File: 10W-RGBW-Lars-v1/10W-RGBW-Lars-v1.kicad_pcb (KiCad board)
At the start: 4 copper layers, 47.1 x 43.3 mm, 133 parts, among them J1 USB_C_Receptacle_USB2.0_16P, J101 Conn_Coaxial, J601 Screw_Terminal_01x02, SW1 SW_SPST, SW2 SW_SPST, U1 CH224D, U101 ESP32-C6FHx, U202 TPS92201, U302 TPS92201, U402 TPS92201, U502 TPS92201, U601 MB34F, U602 SY8366H, U603 XBL1117, Y1 40MHz

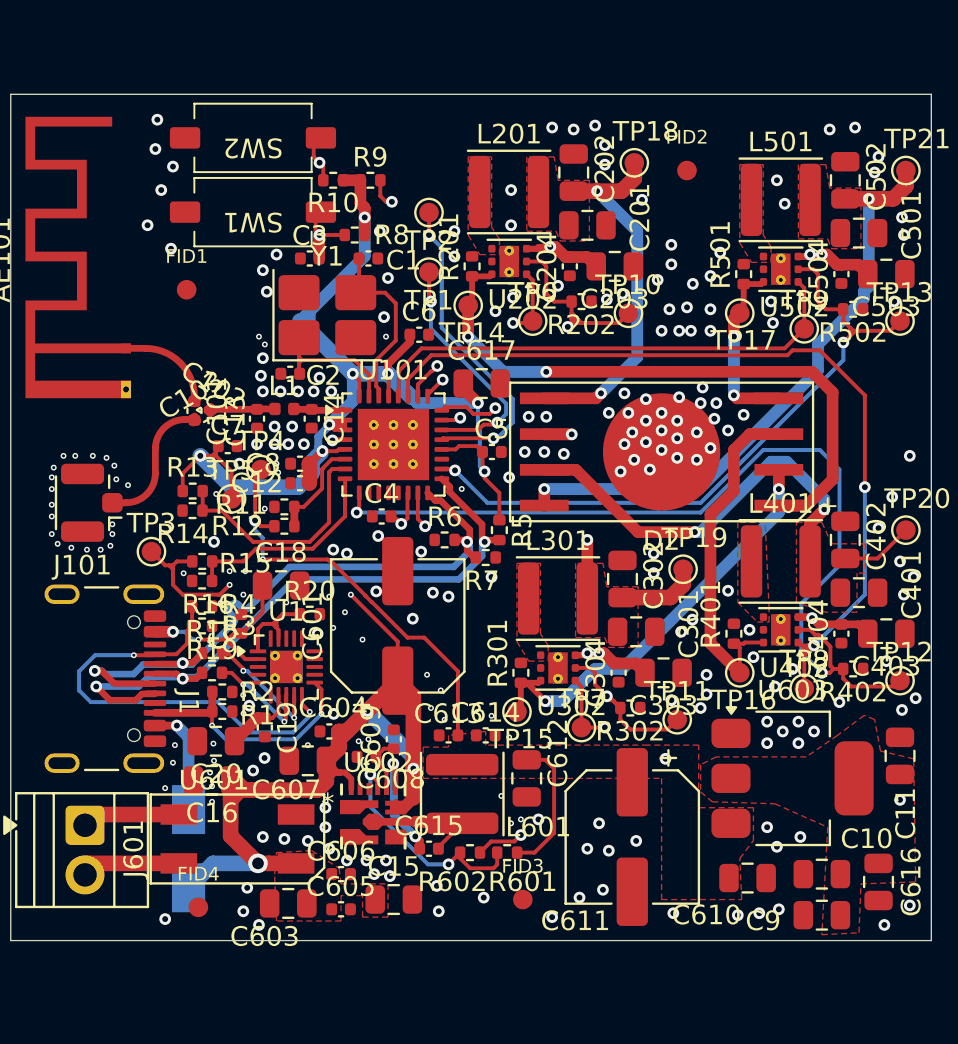
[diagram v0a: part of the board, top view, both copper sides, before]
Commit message: added fiducials, fixed shunt resistor size
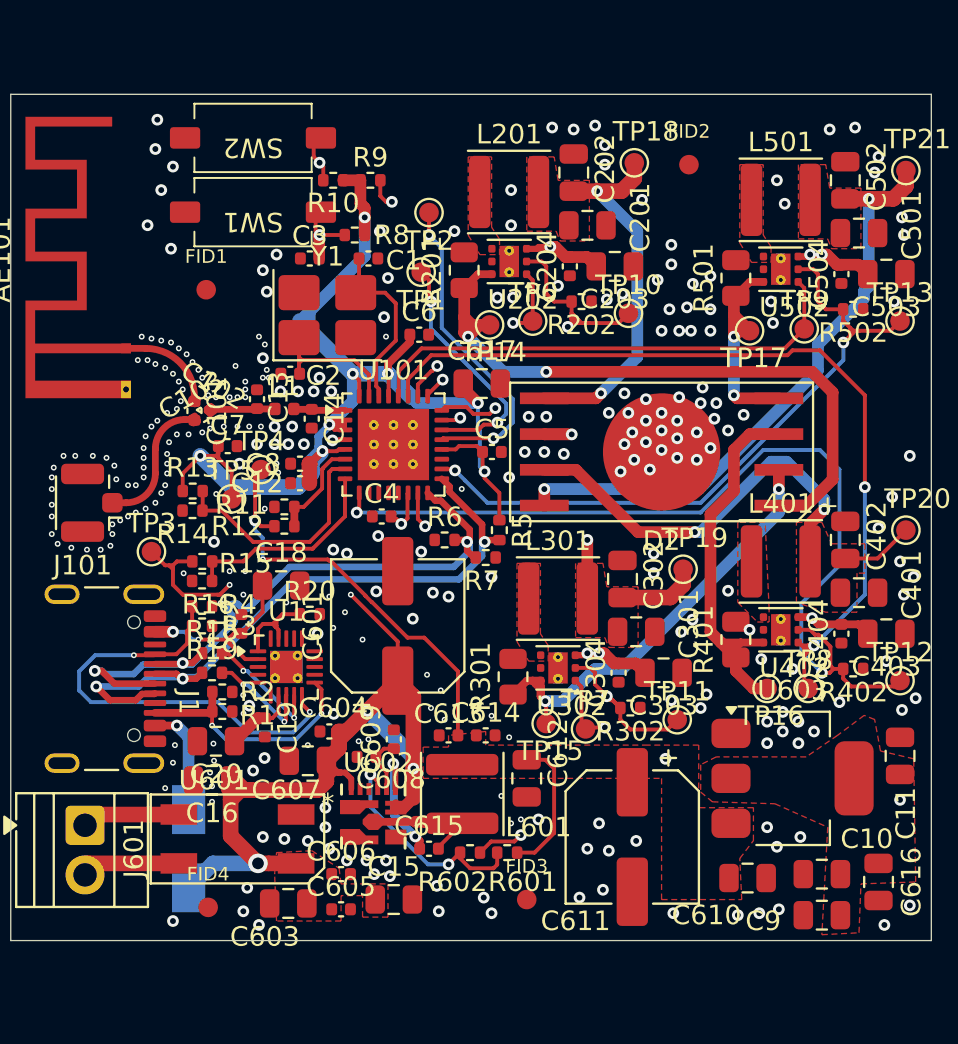
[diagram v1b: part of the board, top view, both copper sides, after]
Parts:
- R201, R301, R401, R501: value 100m -> 100m 250mW; footprint Resistor_SMD:R_0402_1005Metric -> Resistor_SMD:R_0805_2012Metric
- moved TP16 1.61 mm to (143.8, 68.9)
- moved TP15 1.61 mm to (132.5, 70.7)
- moved TP14 1.48 mm to (129.6, 50.3)
- moved TP17 1.03 mm to (142.9, 50.6)
- moved C13 1.00 mm to (117.7, 54.1), turned to 90 degrees
- moved FID1 1.00 mm to (115.1, 48.5)
- moved FID4 0.50 mm to (115.2, 80.1)
- moved R201 0.45 mm to (128.3, 47.5)
- moved R501 0.45 mm to (142.2, 47.9)
- moved R301 0.45 mm to (130.8, 68.3)
- moved TP1 0.40 mm to (126.1, 47.6)
- moved R401 0.32 mm to (142.2, 66.4)
- moved FID2 0.32 mm to (139.8, 42.1)
- moved TP7 0.22 mm to (134.5, 71.0)
- moved TP8 0.20 mm to (145.9, 68.9)
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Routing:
- net /LedDriverRed/LED-: track 31.5 -> 34.7 mm
- net /LedDriverWhite/LED-: track 9.04 -> 11.3 mm
- net /LedDriverBlue/LED-: track 18.3 -> 20.0 mm
- net /LedDriverGreen/LED-: track 22.1 -> 23.7 mm
- net GND: vias 239 -> 292
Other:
- board text added: "PCB specification: Number of copper layers: 4 Stackup: JLC04161H-7628 Dielectric material: FR-4 Finished PCB thickness: 1.6mm Finished copper thickness outer layers: 35um Finished copper thickness inner layers: 15um Soldermask: green Silkscreen: white ROHS compliant: yes Surface finish: LeadFree HASL"
